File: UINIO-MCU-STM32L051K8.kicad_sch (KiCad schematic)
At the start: 26 parts, among them J1 Conn_01x14_Male, J2 Conn_01x14_Male, J3 Conn_01x04_Male, SW1 SW_Push, SW2 SW_Push, U1 ME6211C33M5G-N, U2 W25Q128JVSSIQ, U3 STM32L051K8U6, Y1 Crystal_GND24

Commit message: Rename all of files.
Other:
- title: UINIO-EVB-STM32L051K8 -> UINIO-MCU-STM32L051K8
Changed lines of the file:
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@@
   (paper "A4")
   (title_block
-    (title "UINIO-EVB-STM32L051K8")
+    (title "UINIO-MCU-STM32L051K8")
     (date "2022-09-29")
     (rev "Hank")

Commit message: Update PCB layout.
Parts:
- C10, C11: value 8pF -> 22pF
- Y1: value Crystal_GND24 -> 12MHz
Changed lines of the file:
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@@
     (in_bom yes) (on_board yes)
     (property "Reference" "C10" (id 0) (at 261.874 64.008 90))
-    (property "Value" "8pF" (id 1) (at 261.874 60.452 90))
+    (property "Value" "22pF" (id 1) (at 262.89 60.325 90))
     (property "Footprint" "Capacitor_SMD:C_0402_1005Metric" (id 2) (at 255.27 61.2648 0)
       (effects (font (size 1.27 1.27)) hide)
@@
     (in_bom yes) (on_board yes)
     (property "Reference" "Y1" (id 0) (at 242.57 59.69 90))
-    (property "Value" "Crystal_GND24" (id 1) (at 242.57 72.39 90))
+    (property "Value" "12MHz" (id 1) (at 242.57 72.39 90))
     (property "Footprint" "Crystal:Crystal_SMD_3225-4Pin_3.2x2.5mm" (id 2) (at 242.57 66.04 0)
       (effects (font (size 1.27 1.27)) hide)
@@
     (in_bom yes) (on_board yes)
     (property "Reference" "C11" (id 0) (at 261.874 71.628 90))
-    (property "Value" "8pF" (id 1) (at 261.874 68.072 90))
+    (property "Value" "22pF" (id 1) (at 262.89 67.945 90))
     (property "Footprint" "Capacitor_SMD:C_0402_1005Metric" (id 2) (at 255.27 68.8848 0)
       (effects (font (size 1.27 1.27)) hide)
@@
     )
     (path "/04927899-643a-465f-a90f-2fe0fcac3f7d"
-      (reference "C10") (unit 1) (value "8pF") (footprint "Capacitor_SMD:C_0402_1005Metric")
+      (reference "C10") (unit 1) (value "22pF") (footprint "Capacitor_SMD:C_0402_1005Metric")
     )
     (path "/4fa74506-c2c7-4363-ba60-ed462593bd01"
-      (reference "C11") (unit 1) (value "8pF") (footprint "Capacitor_SMD:C_0402_1005Metric")
+      (reference "C11") (unit 1) (value "22pF") (footprint "Capacitor_SMD:C_0402_1005Metric")
     )
     (path "/247e2303-24d7-4ed1-8e48-01c05cb88b4f"
@@
     )
     (path "/0b035f2d-2743-477a-82f5-d45d1e5e79ee"
-      (reference "Y1") (unit 1) (value "Crystal_GND24") (footprint "Crystal:Crystal_SMD_3225-4Pin_3.2x2.5mm")
-    )
-  )
+      (reference "Y1") (unit 1) (value "12MHz") (footprint "Crystal:Crystal_SMD_3225-4Pin_3.2x2.5mm")
+    )
+  )

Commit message: Update PCB board.
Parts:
- removed Y1: 12MHz, Crystal:Crystal_SMD_3225-4Pin_3.2x2.5mm, symbol Device:Crystal_GND24
- added Y1: FC135-32.768, Uinio:CRYSTAL-FC135-32.768, symbol Uinio:FC135-32.768
- C10, C11: value 22pF -> 6pF
- USB1: SuppliersPartNumber C720626 -> (none); uuid std:b7acd529d33a47cc95d24e0d290fc457 -> std:2c2510636cee4069ad38e03b5f14209b
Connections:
- net at C10.2, U3.2 (PC14-OSC_IN): now also Y1.2 (GND)
- net at C11.2, U3.3 (PC15-OSC_OUT): now also Y1.1

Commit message: Update PCB Layout.
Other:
- moved on the sheet: F1, Y1
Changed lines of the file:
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@@
   (junction (at 91.44 93.98) (diameter 0) (color 0 0 0 0)
   )
-  (junction (at 44.45 147.32) (diameter 0) (color 0 0 0 0)
-  )
-  (junction (at 236.855 62.23) (diameter 0) (color 0 0 0 0)
+  (junction (at 237.49 62.23) (diameter 0) (color 0 0 0 0)
   )
   (junction (at 194.31 33.02) (diameter 0) (color 0 0 0 0)
@@
   (junction (at 91.44 81.28) (diameter 0) (color 0 0 0 0)
   )
+  (junction (at 35.56 148.59) (diameter 0) (color 0 0 0 0)
+  )
   (junction (at 255.27 88.9) (diameter 0) (color 0 0 0 0)
   )
@@
   (junction (at 97.79 149.86) (diameter 0) (color 0 0 0 0)
   )
-  (junction (at 35.56 147.32) (diameter 0) (color 0 0 0 0)
-  )
   (junction (at 194.31 27.94) (diameter 0) (color 0 0 0 0)
   )
+  (junction (at 44.45 148.59) (diameter 0) (color 0 0 0 0)
+  )
   (junction (at 97.79 148.59) (diameter 0) (color 0 0 0 0)
   )
   (junction (at 50.8 50.8) (diameter 0) (color 0 0 0 0)
   )
-  (junction (at 236.855 69.85) (diameter 0) (color 0 0 0 0)
+  (junction (at 237.49 69.85) (diameter 0) (color 0 0 0 0)
   )
   (junction (at 86.36 43.18) (diameter 0) (color 0 0 0 0)
@@
     (stroke (width 0) (type default) (color 0 0 0 0))
   )
-  (wire (pts (xy 236.855 69.85) (xy 255.27 69.85))
+  (wire (pts (xy 237.49 69.85) (xy 255.27 69.85))
     (stroke (width 0) (type default) (color 0 0 0 0))
   )
@@
     (stroke (width 0) (type default) (color 0 0 0 0))
   )
-  (wire (pts (xy 35.56 147.32) (xy 35.56 151.13))
-    (stroke (width 0) (type default) (color 0 0 0 0))
-  )
   (polyline (pts (xy 17.78 19.05) (xy 17.78 68.58))
     (stroke (width 0) (type default) (color 0 0 0 0))
@@
     (stroke (width 0) (type default) (color 0 0 0 0))
   )
+  (wire (pts (xy 35.56 148.59) (xy 35.56 151.13))
+    (stroke (width 0) (type default) (color 0 0 0 0))
+  )
   (wire (pts (xy 44.45 144.78) (xy 76.2 144.78))
     (stroke (width 0) (type default) (color 0 0 0 0))
@@
     (stroke (width 0) (type default) (color 0 0 0 0))
   )
-  (wire (pts (xy 226.06 62.23) (xy 236.855 62.23))
+  (wire (pts (xy 226.06 62.23) (xy 237.49 62.23))
     (stroke (width 0) (type default) (color 0 0 0 0))
   )
@@
     (stroke (width 0) (type default) (color 0 0 0 0))
   )
+  (wire (pts (xy 44.45 148.59) (xy 44.45 152.4))
+    (stroke (width 0) (type default) (color 0 0 0 0))
+  )
   (wire (pts (xy 34.29 99.06) (xy 35.56 99.06))
     (stroke (width 0) (type default) (color 0 0 0 0))
@@
     (stroke (width 0) (type default) (color 0 0 0 0))
   )
-  (wire (pts (xy 44.45 147.32) (xy 44.45 152.4))
-    (stroke (width 0) (type default) (color 0 0 0 0))
-  )
   (wire (pts (xy 35.56 167.64) (xy 35.56 168.91))
     (stroke (width 0) (type default) (color 0 0 0 0))
@@
     (stroke (width 0) (type default) (color 0 0 0 0))
   )
-  (wire (pts (xy 226.06 69.85) (xy 236.855 69.85))
+  (wire (pts (xy 226.06 69.85) (xy 237.49 69.85))
     (stroke (width 0) (type default) (color 0 0 0 0))
   )
@@
     (stroke (width 0) (type default) (color 0 0 0 0))
   )
-  (wire (pts (xy 44.45 144.78) (xy 44.45 147.32))
+  (wire (pts (xy 44.45 144.78) (xy 44.45 148.59))
     (stroke (width 0) (type default) (color 0 0 0 0))
   )
@@
     (stroke (width 0) (type default) (color 0 0 0 0))
   )
-  (wire (pts (xy 35.56 147.32) (xy 35.56 139.7))
+  (wire (pts (xy 35.56 139.7) (xy 35.56 148.59))
     (stroke (width 0) (type default) (color 0 0 0 0))
   )
@@
     (stroke (width 0) (type default) (color 0 0 0 0))
   )
-  (wire (pts (xy 236.855 62.23) (xy 255.27 62.23))
+  (wire (pts (xy 237.49 62.23) (xy 255.27 62.23))
     (stroke (width 0) (type default) (color 0 0 0 0))
   )
@@
     (stroke (width 0) (type default) (color 0 0 0 0))
   )
-  (wire (pts (xy 43.18 147.32) (xy 44.45 147.32))
+  (wire (pts (xy 43.18 148.59) (xy 44.45 148.59))
     (stroke (width 0) (type default) (color 0 0 0 0))
   )
@@
     (pin "5")
   )
-  (symbol (lib_id "Uinio:FC135-32.768") (at 236.855 64.77 90) (unit 1)
+  (symbol (lib_id "Uinio:FC135-32.768") (at 237.49 64.77 90) (unit 1)
     (in_bom yes) (on_board yes) (fields_autoplaced)
-    (property "Reference" "Y1" (id 0) (at 240.03 64.7699 90)
-      (effects (font (size 1.27 1.27)) (justify right))
-    )
-    (property "Value" "FC135-32.768" (id 1) (at 240.03 67.3099 90)
-      (effects (font (size 1.27 1.27)) (justify right))
-    )
-    (property "Footprint" "Uinio:CRYSTAL-FC135-32.768" (id 2) (at 236.8296 64.77 0)
-      (effects (font (size 1.27 1.27)) hide)
-    )
-    (property "Datasheet" "" (id 3) (at 241.9096 64.77 0)
-      (effects (font (size 1.27 1.27)) hide)
-    )
-    (property "SuppliersPartNumber" "C1986919" (id 4) (at 246.9896 64.77 0)
-      (effects (font (size 1.27 1.27)) hide)
-    )
-    (property "uuid" "std:1a7d7ec5dddf46f9929a2236d62d3241" (id 5) (at 246.9896 64.77 0)
+    (property "Reference" "Y1" (id 0) (at 240.665 64.7699 90)
+      (effects (font (size 1.27 1.27)) (justify right))
+    )
+    (property "Value" "FC135-32.768" (id 1) (at 240.665 67.3099 90)
+      (effects (font (size 1.27 1.27)) (justify right))
+    )
+    (property "Footprint" "Uinio:CRYSTAL-FC135-32.768" (id 2) (at 237.4646 64.77 0)
+      (effects (font (size 1.27 1.27)) hide)
+    )
+    (property "Datasheet" "" (id 3) (at 242.5446 64.77 0)
+      (effects (font (size 1.27 1.27)) hide)
+    )
+    (property "SuppliersPartNumber" "C1986919" (id 4) (at 247.6246 64.77 0)
+      (effects (font (size 1.27 1.27)) hide)
+    )
+    (property "uuid" "std:1a7d7ec5dddf46f9929a2236d62d3241" (id 5) (at 247.6246 64.77 0)
       (effects (font (size 1.27 1.27)) hide)
     )
@@
     (pin "9")
   )
-  (symbol (lib_id "Device:Polyfuse") (at 39.37 147.32 270) (unit 1)
-    (in_bom yes) (on_board yes)
-    (property "Reference" "F1" (id 0) (at 38.1 144.78 90)
+  (symbol (lib_id "Device:Polyfuse") (at 39.37 148.59 270) (unit 1)
+    (in_bom yes) (on_board yes)
+    (property "Reference" "F1" (id 0) (at 38.1 146.05 90)
       (effects (font (size 1.27 1.27)) (justify left))
     )
-    (property "Value" "Polyfuse" (id 1) (at 35.56 149.86 90)
+    (property "Value" "Polyfuse" (id 1) (at 35.56 151.13 90)
       (effects (font (size 1.27 1.27)) (justify left))
     )
-    (property "Footprint" "Fuse:Fuse_1206_3216Metric" (id 2) (at 34.29 148.59 0)
+    (property "Footprint" "Fuse:Fuse_1206_3216Metric" (id 2) (at 34.29 149.86 0)
       (effects (font (size 1.27 1.27)) (justify left) hide)
     )
-    (property "Datasheet" "~" (id 3) (at 39.37 147.32 0)
-      (effects (font (size 1.27 1.27)) hide)
-    )
+    (property "Datasheet" "~" (id 3) (at 39.37 148.59 0)
+      (effects (font (size 1.27 1.27)) hide)
+    )

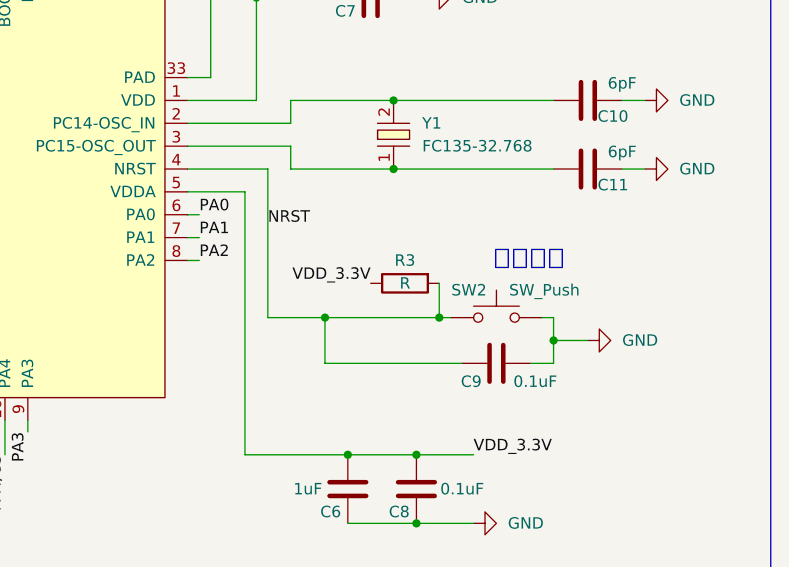
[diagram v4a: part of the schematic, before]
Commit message: Update capacitance value.
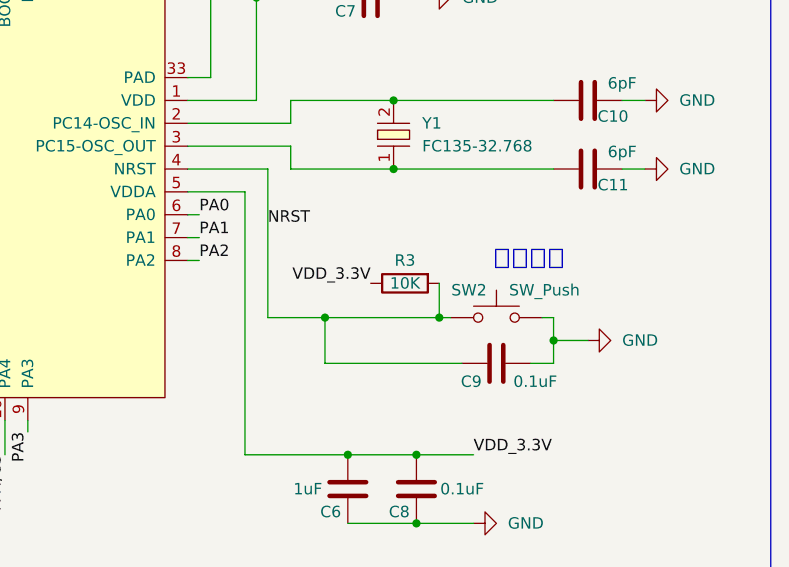
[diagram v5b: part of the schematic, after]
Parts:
- R3: value R -> 10K
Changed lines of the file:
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@@
     (in_bom yes) (on_board yes)
     (property "Reference" "R3" (id 0) (at 238.76 80.01 90))
-    (property "Value" "R" (id 1) (at 238.76 82.55 90))
+    (property "Value" "10K" (id 1) (at 238.76 82.55 90))
     (property "Footprint" "Resistor_SMD:R_0402_1005Metric" (id 2) (at 238.76 80.772 90)
       (effects (font (size 1.27 1.27)) hide)
@@
     )
     (path "/0dc4dc38-298e-43a4-a369-891beafa0569"
-      (reference "R3") (unit 1) (value "R") (footprint "Resistor_SMD:R_0402_1005Metric")
+      (reference "R3") (unit 1) (value "10K") (footprint "Resistor_SMD:R_0402_1005Metric")
     )
     (path "/a26fb178-aeb6-4dfd-8d0f-683b1e6bca57"

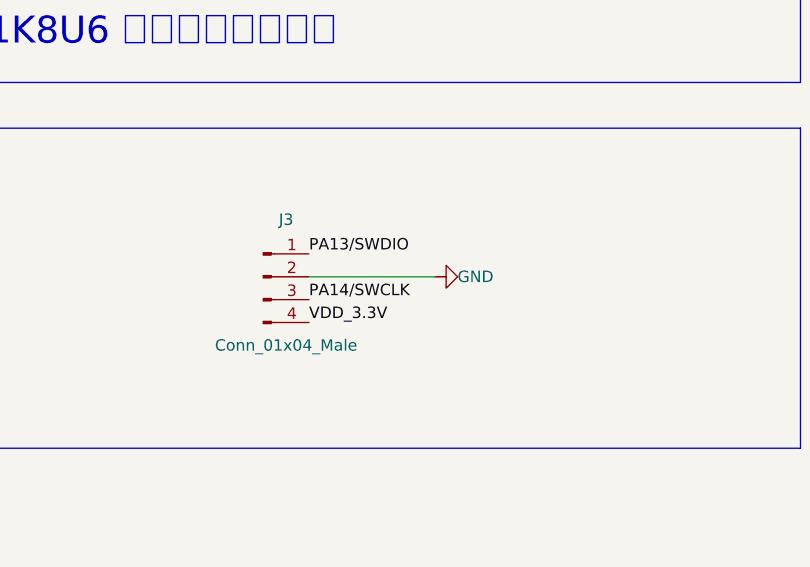
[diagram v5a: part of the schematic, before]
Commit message: Update SWD interface.
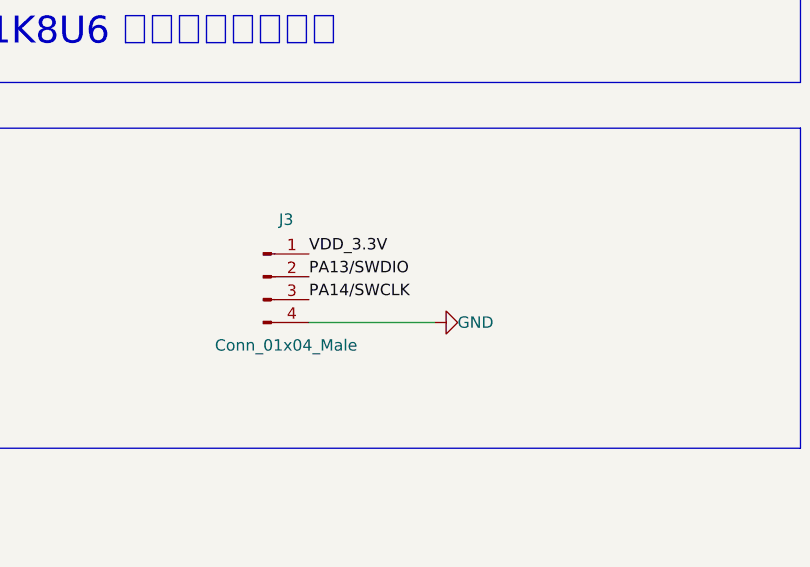
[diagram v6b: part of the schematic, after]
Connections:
- net GND: now also J3.4 (Pin_4); no longer J3.2 (Pin_2)
- net PA13/SWDIO: now also J3.2 (Pin_2); no longer J3.1 (Pin_1)
- net VDD_3.3V: now also J3.1 (Pin_1); no longer J3.4 (Pin_4)
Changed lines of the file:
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@@
     (stroke (width 0) (type default) (color 0 0 0 0))
   )
-  (wire (pts (xy 224.79 143.51) (xy 238.76 143.51))
+  (wire (pts (xy 224.79 148.59) (xy 238.76 148.59))
     (stroke (width 0) (type default) (color 0 0 0 0))
   )
@@
     (effects (font (size 1.27 1.27)) (justify left bottom))
   )
-  (label "PA13{slash}SWDIO" (at 224.79 140.97 0)
+  (label "PA13{slash}SWDIO" (at 224.79 143.51 0)
     (effects (font (size 1.27 1.27)) (justify left bottom))
   )
@@
     (effects (font (size 1.27 1.27)) (justify left bottom))
   )
-  (label "VDD_3.3V" (at 224.79 148.59 0)
+  (label "VDD_3.3V" (at 224.79 140.97 0)
     (effects (font (size 1.27 1.27)) (justify left bottom))
   )
@@
     (pin "2")
   )
-  (symbol (lib_id "power:GND") (at 238.76 143.51 90) (mirror x) (unit 1)
-    (in_bom yes) (on_board yes)
-    (property "Reference" "#PWR015" (id 0) (at 245.11 143.51 0)
-      (effects (font (size 1.27 1.27)) hide)
-    )
-    (property "Value" "GND" (id 1) (at 241.3 143.51 90)
-      (effects (font (size 1.27 1.27)) (justify right))
-    )
-    (property "Footprint" "" (id 2) (at 238.76 143.51 0)
-      (effects (font (size 1.27 1.27)) hide)
-    )
-    (property "Datasheet" "" (id 3) (at 238.76 143.51 0)
-      (effects (font (size 1.27 1.27)) hide)
-    )
+  (symbol (lib_id "power:GND") (at 238.76 148.59 90) (mirror x) (unit 1)
+    (in_bom yes) (on_board yes)
+    (property "Reference" "#PWR015" (id 0) (at 245.11 148.59 0)
+      (effects (font (size 1.27 1.27)) hide)
+    )
+    (property "Value" "GND" (id 1) (at 241.3 148.59 90)
+      (effects (font (size 1.27 1.27)) (justify right))
+    )
+    (property "Footprint" "" (id 2) (at 238.76 148.59 0)
+      (effects (font (size 1.27 1.27)) hide)
+    )
+    (property "Datasheet" "" (id 3) (at 238.76 148.59 0)
+      (effects (font (size 1.27 1.27)) hide)
+    )
